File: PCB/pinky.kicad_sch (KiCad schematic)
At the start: 51 parts, among them SW10 Switch, SW11 Switch, SW12 Switch, SW13 Switch, SW14 Switch, SW15 Switch, SW16 Switch, SW17 Switch, SW18 Switch, SW2 Switch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

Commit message: Mounting holes positioning
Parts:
- removed H5: MountingHole, MountingHole:MountingHole_2.2mm_M2, symbol Pinky:MountingHole
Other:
- moved on the sheet: H1, H2, H3, H4
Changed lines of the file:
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@@
 	(symbol
 		(lib_id "Pinky:MountingHole")
-		(at 170.18 36.322 0)
+		(at 170.18 40.64 0)
 		(unit 1)
 		(body_style 1)
@@
 		(fields_autoplaced yes)
 		(property "Reference" "H3"
-			(at 172.72 35.0519 0)
+			(at 172.72 39.3699 0)
 			(show_name no)
 			(do_not_autoplace no)
@@
 		)
 		(property "Value" "MountingHole"
-			(at 172.72 37.5919 0)
+			(at 172.72 41.9099 0)
 			(show_name no)
 			(do_not_autoplace no)
@@
 		)
 		(property "Footprint" "MountingHole:MountingHole_2.2mm_M2"
-			(at 170.18 36.322 0)
-			(hide yes)
-			(show_name no)
-			(do_not_autoplace no)
-			(effects
-				(font
-					(size 1.27 1.27)
-				)
-			)
-		)
-		(property "Datasheet" ""
-			(at 170.18 36.322 0)
+			(at 170.18 40.64 0)
+			(hide yes)
+			(show_name no)
+			(do_not_autoplace no)
+			(effects
+				(font
+					(size 1.27 1.27)
+				)
+			)
+		)
+		(property "Datasheet" ""
+			(at 170.18 40.64 0)
 			(hide yes)
 			(show_name no)
@@
 		)
 		(property "Description" "Mounting Hole without connection"
-			(at 170.18 36.322 0)
+			(at 170.18 40.64 0)
 			(hide yes)
 			(show_name no)
@@
 	(symbol
 		(lib_id "Pinky:MountingHole")
-		(at 170.18 29.972 0)
+		(at 170.18 34.29 0)
 		(unit 1)
 		(body_style 1)
@@
 		(fields_autoplaced yes)
 		(property "Reference" "H2"
-			(at 172.72 28.7019 0)
+			(at 172.72 33.0199 0)
 			(show_name no)
 			(do_not_autoplace no)
@@
 		)
 		(property "Value" "MountingHole"
-			(at 172.72 31.2419 0)
+			(at 172.72 35.5599 0)
 			(show_name no)
 			(do_not_autoplace no)
@@
 		)
 		(property "Footprint" "MountingHole:MountingHole_2.2mm_M2"
-			(at 170.18 29.972 0)
-			(hide yes)
-			(show_name no)
-			(do_not_autoplace no)
-			(effects
-				(font
-					(size 1.27 1.27)
-				)
-			)
-		)
-		(property "Datasheet" ""
-			(at 170.18 29.972 0)
+			(at 170.18 34.29 0)
+			(hide yes)
+			(show_name no)
+			(do_not_autoplace no)
+			(effects
+				(font
+					(size 1.27 1.27)
+				)
+			)
+		)
+		(property "Datasheet" ""
+			(at 170.18 34.29 0)
 			(hide yes)
 			(show_name no)
@@
 		)
 		(property "Description" "Mounting Hole without connection"
-			(at 170.18 29.972 0)
+			(at 170.18 34.29 0)
 			(hide yes)
 			(show_name no)
@@
 	(symbol
 		(lib_id "Pinky:MountingHole")
-		(at 170.18 23.622 0)
+		(at 170.18 27.94 0)
 		(unit 1)
 		(body_style 1)
@@
 		(fields_autoplaced yes)
 		(property "Reference" "H1"
-			(at 172.72 22.3519 0)
+			(at 172.72 26.6699 0)
 			(show_name no)
 			(do_not_autoplace no)
@@
 		)
 		(property "Value" "MountingHole"
-			(at 172.72 24.8919 0)
+			(at 172.72 29.2099 0)
 			(show_name no)
 			(do_not_autoplace no)
@@
 		)
 		(property "Footprint" "MountingHole:MountingHole_2.2mm_M2"
-			(at 170.18 23.622 0)
-			(hide yes)
-			(show_name no)
-			(do_not_autoplace no)
-			(effects
-				(font
-					(size 1.27 1.27)
-				)
-			)
-		)
-		(property "Datasheet" ""
-			(at 170.18 23.622 0)
+			(at 170.18 27.94 0)
+			(hide yes)
+			(show_name no)
+			(do_not_autoplace no)
+			(effects
+				(font
+					(size 1.27 1.27)
+				)
+			)
+		)
+		(property "Datasheet" ""
+			(at 170.18 27.94 0)
 			(hide yes)
 			(show_name no)
@@
 		)
 		(property "Description" "Mounting Hole without connection"
-			(at 170.18 23.622 0)
+			(at 170.18 27.94 0)
 			(hide yes)
 			(show_name no)
@@
 	)
 	(symbol
-		(lib_id "Pinky:MountingHole")
-		(at 170.18 49.53 0)
-		(unit 1)
-		(body_style 1)
-		(exclude_from_sim no)
-		(in_bom no)
-		(on_board yes)
-		(in_pos_files yes)
-		(dnp no)
-		(fields_autoplaced yes)
-		(property "Reference" "H5"
-			(at 172.72 48.2599 0)
-			(show_name no)
-			(do_not_autoplace no)
-			(effects
-				(font
-					(size 1.27 1.27)
-				)
-				(justify left)
-			)
-		)
-		(property "Value" "MountingHole"
-			(at 172.72 50.7999 0)
-			(show_name no)
-			(do_not_autoplace no)
-			(effects
-				(font
-					(size 1.27 1.27)
-				)
-				(justify left)
-			)
-		)
-		(property "Footprint" "MountingHole:MountingHole_2.2mm_M2"
-			(at 170.18 49.53 0)
-			(hide yes)
-			(show_name no)
-			(do_not_autoplace no)
-			(effects
-				(font
-					(size 1.27 1.27)
-				)
-			)
-		)
-		(property "Datasheet" ""
-			(at 170.18 49.53 0)
-			(hide yes)
-			(show_name no)
-			(do_not_autoplace no)
-			(effects
-				(font
-					(size 1.27 1.27)
-				)
-			)
-		)
-		(property "Description" "Mounting Hole without connection"
-			(at 170.18 49.53 0)
-			(hide yes)
-			(show_name no)
-			(do_not_autoplace no)
-			(effects
-				(font
-					(size 1.27 1.27)
-				)
-			)
-		)
-		(instances
-			(project "pinky"
-				(path "/231ead31-262f-44fe-a25c-f58d2465dcca"
-					(reference "H5")
-					(unit 1)
-				)
-			)
-		)
-	)
-	(symbol
 		(lib_id "Pinky:Switch")
 		(at 119.38 69.85 0)
@@
 	(symbol
 		(lib_id "Pinky:MountingHole")
-		(at 170.18 42.926 0)
+		(at 170.18 47.244 0)
 		(unit 1)
 		(body_style 1)
@@
 		(fields_autoplaced yes)
 		(property "Reference" "H4"
-			(at 172.72 41.6559 0)
+			(at 172.72 45.9739 0)
 			(show_name no)
 			(do_not_autoplace no)
@@
 		)
 		(property "Value" "MountingHole"
-			(at 172.72 44.1959 0)
+			(at 172.72 48.5139 0)
 			(show_name no)
 			(do_not_autoplace no)
@@
 		)
 		(property "Footprint" "MountingHole:MountingHole_2.2mm_M2"
-			(at 170.18 42.926 0)
-			(hide yes)
-			(show_name no)
-			(do_not_autoplace no)
-			(effects
-				(font
-					(size 1.27 1.27)
-				)
-			)
-		)
-		(property "Datasheet" ""
-			(at 170.18 42.926 0)
+			(at 170.18 47.244 0)
+			(hide yes)
+			(show_name no)
+			(do_not_autoplace no)
+			(effects
+				(font
+					(size 1.27 1.27)
+				)
+			)
+		)
+		(property "Datasheet" ""
+			(at 170.18 47.244 0)
 			(hide yes)
 			(show_name no)
@@
 		)
 		(property "Description" "Mounting Hole without connection"
-			(at 170.18 42.926 0)
-			(hide yes)
-			(show_name no)
+			(at 170.18 47.244 0)
+			(hide yes)
+			(show_name no)

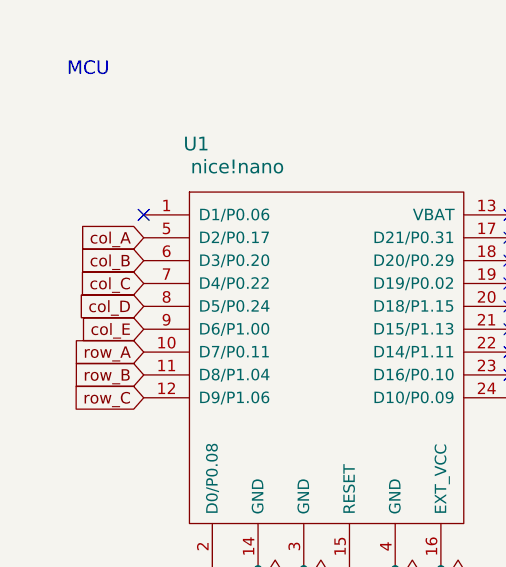
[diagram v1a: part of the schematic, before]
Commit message: Pins reordering to aid routing
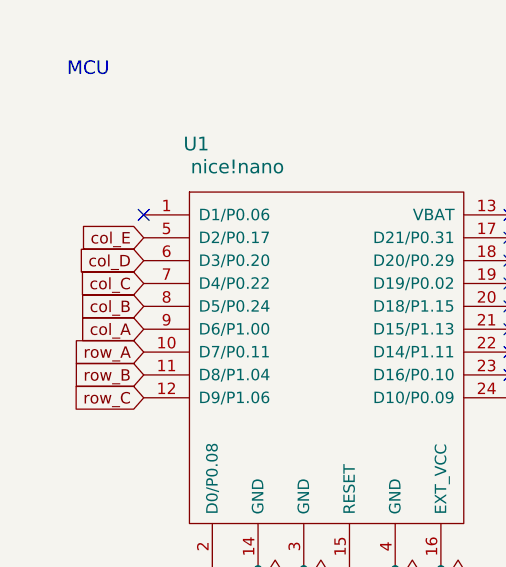
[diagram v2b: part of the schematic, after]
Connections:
- net col_A: now also U1.9 (D6/P1.00); no longer U1.5 (D2/P0.17)
- net col_B: now also U1.8 (D5/P0.24); no longer U1.6 (D3/P0.20)
- net col_D: now also U1.6 (D3/P0.20); no longer U1.8 (D5/P0.24)
- net col_E: now also U1.5 (D2/P0.17); no longer U1.9 (D6/P1.00)
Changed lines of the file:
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@@
 	(global_label "col_E"
 		(shape input)
-		(at 25.4 48.26 180)
+		(at 25.4 38.1 180)
 		(fields_autoplaced yes)
 		(effects
@@
 		)
 		(property "Intersheetrefs" "${INTERSHEET_REFS}"
-			(at 17.3954 48.26 0)
+			(at 17.3954 38.1 0)
 			(hide yes)
 			(show_name no)
@@
 	(global_label "col_A"
 		(shape input)
-		(at 25.4 38.1 180)
+		(at 25.4 48.26 180)
 		(fields_autoplaced yes)
 		(effects
@@
 		)
 		(property "Intersheetrefs" "${INTERSHEET_REFS}"
-			(at 17.4558 38.1 0)
+			(at 17.4558 48.26 0)
 			(hide yes)
 			(show_name no)
@@
 	(global_label "col_D"
 		(shape input)
-		(at 25.4 45.72 180)
+		(at 25.4 40.64 180)
 		(fields_autoplaced yes)
 		(effects
@@
 		)
 		(property "Intersheetrefs" "${INTERSHEET_REFS}"
-			(at 17.2744 45.72 0)
+			(at 17.2744 40.64 0)
 			(hide yes)
 			(show_name no)
@@
 	(global_label "col_B"
 		(shape input)
-		(at 25.4 40.64 180)
+		(at 25.4 45.72 180)
 		(fields_autoplaced yes)
 		(effects
@@
 		)
 		(property "Intersheetrefs" "${INTERSHEET_REFS}"
-			(at 17.2744 40.64 0)
+			(at 17.2744 45.72 0)
 			(hide yes)
 			(show_name no)
